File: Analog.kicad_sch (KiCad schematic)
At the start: 42 parts, among them IC1 AMC1350DWVR, IC2 AMC1350DWVR, IC3 ZXRE160AET5TA, U2 TLV9001IDBVR, U3 TLV9001IDBVR

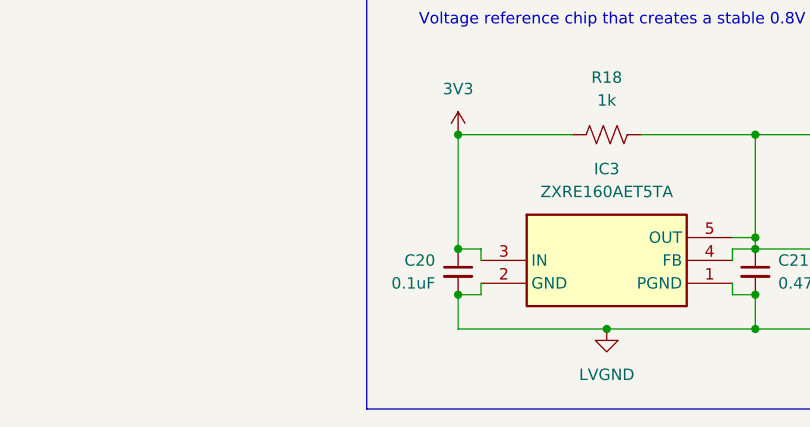
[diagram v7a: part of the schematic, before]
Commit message: Part Numbers fleshed out
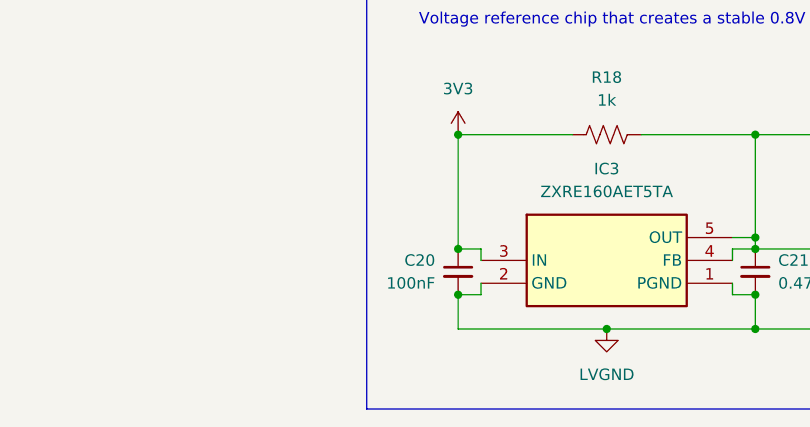
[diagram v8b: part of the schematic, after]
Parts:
- C20: value 0.1uF -> 100nF; P/N MLASU063SB7102KFNA01 -> MLASH168SB7104KTNA01
- IC1, IC2: P/N (none) -> AMC1350DWVR
- IC3: P/N (none) -> ZXRE160
- R11, R21, R23, R26, R27, R9: P/N CRCW0603100KFKEE -> CRCW06032K49FKEAC
- R18: P/N CRCW060310R0FKEE -> CRCW06031K00FKEI
- R19: P/N CRCW060310R0FKEE -> CRCW06035K10FKEC
- R20: P/N CRCW060310R0FKEE -> CRCW060315K0FKEA
- R22, R24, R28, R29: P/N CRCW0603100KFKEE -> CRCW060315K0FKEA
- U2, U3: P/N (none) -> TLV9001IDBVR
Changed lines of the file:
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@@
 			)
 		)
-		(property "P/N" "CRCW0603100KFKEE"
+		(property "P/N" "CRCW060315K0FKEA"
 			(at 217.17 63.5 0)
 			(effects
@@
 			)
 		)
-		(property "P/N" "CRCW0603100KFKEE"
+		(property "P/N" "CRCW060315K0FKEA"
 			(at 238.76 41.91 0)
 			(effects
@@
 			)
 		)
-		(property "P/N" "CRCW060310R0FKEE"
+		(property "P/N" "CRCW060315K0FKEA"
 			(at 156.21 149.86 90)
 			(effects
@@
 			)
 		)
-		(property "Value" "0.1uF"
+		(property "Value" "100nF"
 			(at 109.22 148.5962 0)
 			(effects
@@
 			)
 		)
-		(property "P/N" "MLASU063SB7102KFNA01"
+		(property "P/N" "MLASH168SB7104KTNA01"
 			(at 111.76 147.32 0)
 			(effects
@@
 			)
 		)
+		(property "P/N" "AMC1350DWVR"
+			(at 127 81.28 0)
+			(effects
+				(font
+					(size 1.27 1.27)
+				)
+				(hide yes)
+			)
+		)
 		(pin "6"
 		)
@@
 			)
 		)
+		(property "P/N" "TLV9001IDBVR"
+			(at 232.41 57.15 0)
+			(effects
+				(font
+					(size 1.27 1.27)
+				)
+				(hide yes)
+			)
+		)
 		(pin "4"
 		)
@@
 			)
 		)
-		(property "P/N" "CRCW060310R0FKEE"
+		(property "P/N" "CRCW06035K10FKEC "
 			(at 156.21 140.97 90)
 			(effects
@@
 			)
 		)
+		(property "P/N" "ZXRE160"
+			(at 114.3 143.51 0)
+			(effects
+				(font
+					(size 1.27 1.27)
+				)
+				(hide yes)
+			)
+		)
 		(pin "1"
 		)
@@
 			)
 		)
-		(property "P/N" "CRCW0603100KFKEE"
+		(property "P/N" "CRCW060315K0FKEA"
 			(at 240.03 81.28 0)
 			(effects
@@
 			)
 		)
-		(property "P/N" "CRCW0603100KFKEE"
+		(property "P/N" "CRCW06032K49FKEAC"
 			(at 212.09 99.06 0)
 			(effects
@@
 			)
 		)
-		(property "P/N" "CRCW0603100KFKEE"
+		(property "P/N" "CRCW06032K49FKEAC"
 			(at 212.09 54.61 0)
 			(effects
@@
 			)
 		)
+		(property "P/N" "TLV9001IDBVR"
+			(at 232.41 96.52 0)
+			(effects
+				(font
+					(size 1.27 1.27)
+				)
+				(hide yes)
+			)
+		)
 		(pin "4"
 		)
@@
 			)
 		)
-		(property "P/N" "CRCW0603100KFKEE"
+		(property "P/N" "CRCW06032K49FKEAC"
 			(at 212.09 93.98 0)
 			(effects
@@
 			)
 		)
-		(property "P/N" "CRCW0603100KFKEE"
+		(property "P/N" "CRCW06032K49FKEAC"
 			(at 66.04 62.23 0)
 			(effects
@@
 			)
 		)
-		(property "P/N" "CRCW0603100KFKEE"
+		(property "P/N" "CRCW06032K49FKEAC"
 			(at 212.09 59.69 0)
 			(effects
@@
 			)
 		)
-		(property "P/N" "CRCW0603100KFKEE"
+		(property "P/N" "CRCW060315K0FKEA"
 			(at 217.17 102.87 0)
 			(effects
@@
 			)
 		)
+		(property "P/N" "AMC1350DWVR"
+			(at 127 45.72 0)
+			(effects
+				(font
+					(size 1.27 1.27)
+				)
+				(hide yes)
+			)
+		)
 		(pin "6"
 		)
@@
 			)
 		)
-		(property "P/N" "CRCW0603100KFKEE"
+		(property "P/N" "CRCW06032K49FKEAC"
 			(at 36.83 62.23 0)
 			(effects
@@
 			)
 		)
-		(property "P/N" "CRCW060310R0FKEE"
+		(property "P/N" "CRCW06031K00FKEI "
 			(at 128.27 132.08 90)
 			(effects
